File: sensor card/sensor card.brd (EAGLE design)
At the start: 100 x 80 mm, 30 parts, among them J1 MJ-3536N, J2 MJ-3536N, X1 S4B-XH-A, X2 S4B-XH-A

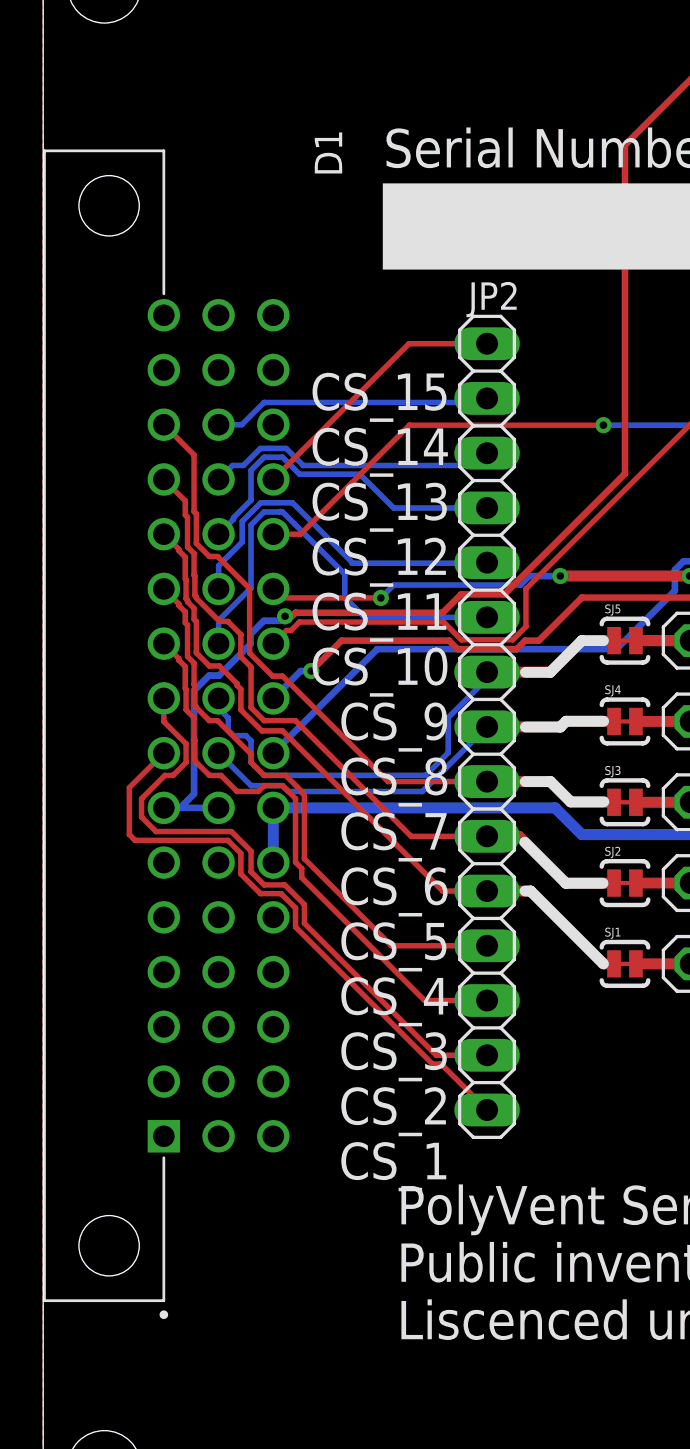
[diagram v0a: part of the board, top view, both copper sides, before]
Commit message: got rid of a 0.05mm offset in the position of the din41612 connectors
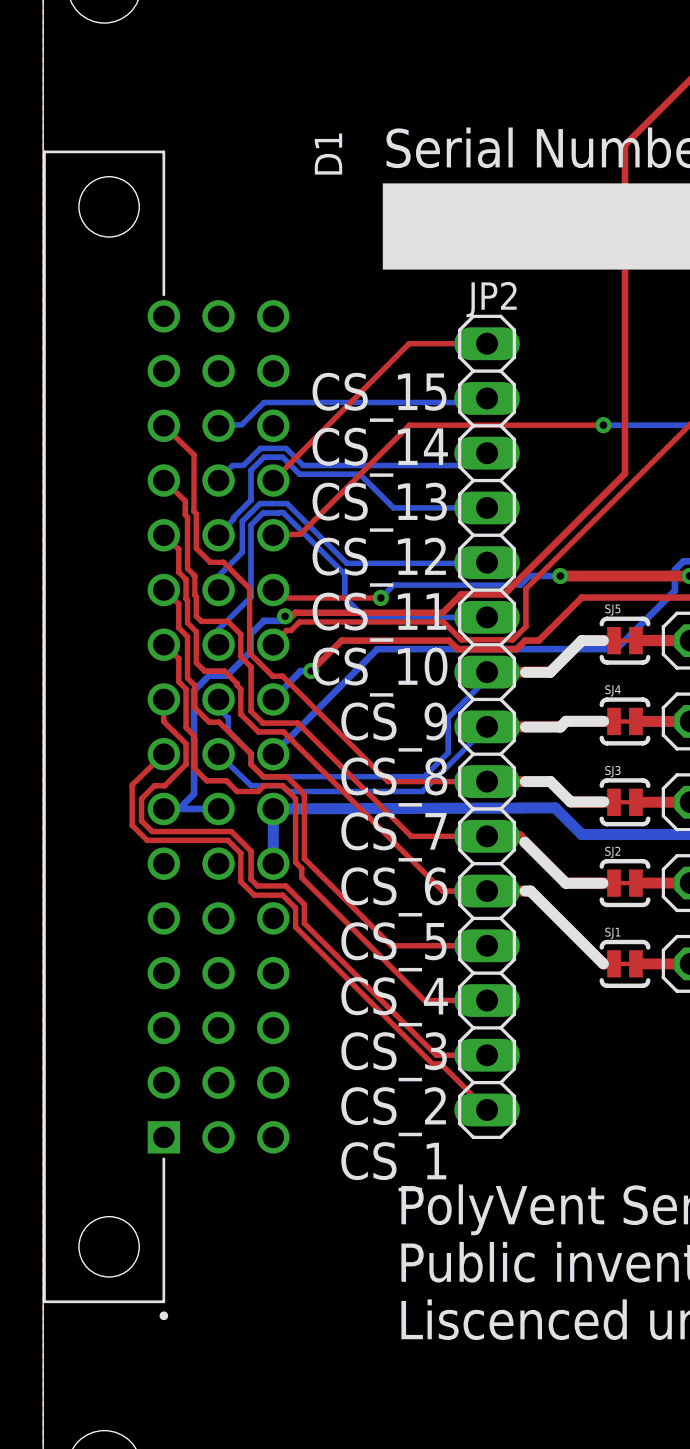
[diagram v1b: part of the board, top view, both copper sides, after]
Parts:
- moved D1 0.05 mm to (5.60, 20.9)
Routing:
- net CS_6: track 32.7 -> 33.3 mm
